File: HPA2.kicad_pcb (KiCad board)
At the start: 2 copper layers, 101.6 x 73 mm, 120 parts, among them J1 Input, J2 Conn_01x01_Male, J3 Power, J4 Output, J5 Mute, K1 G6H-2, Q1 BC560C, Q10 BC560C, Q11 BC560C, Q12 BC550C, Q13 BC550C, Q14 KSC1845, Q15 BC550C, Q16 BC560C, Q17 KSA992, Q18 BC560C, Q19 BC550C, Q2 BC560C, Q20 BC560C, Q21 BC550C, Q22 TTA004B, Q23 TTA004B, Q24 TTC004B, Q25 TTC004B, Q26 KSC2690AY, Q27 KSA1220AY, Q3 BC549C, Q4 BC549C, Q5 BC549C, Q6 BC560C, Q7 BC549C, Q8 BC560C, Q9 BC560C, U1 2N5564, U2 LT1761-BYP, U3 LT1964-BYP, U4 ADA4627-1

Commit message: Copied TO-126-3-Vertical footprint into project-local library and updated board.
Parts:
- Q22, Q23, Q24, Q25, Q26, Q27: footprint Package_TO_SOT_THT:TO-126-3_Vertical -> HPA2-footprints:TO-126-3_Vertical
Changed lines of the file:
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@@
 		)
 	)
-	(footprint "Package_TO_SOT_THT:TO-126-3_Vertical"
+	(footprint "HPA2-footprints:TO-126-3_Vertical"
 		(layer "F.Cu")
 		(at 163.195 124.46 90)
@@
 		)
 	)
-	(footprint "Package_TO_SOT_THT:TO-126-3_Vertical"
+	(footprint "HPA2-footprints:TO-126-3_Vertical"
 		(layer "F.Cu")
 		(at 163.195 88.9 -90)
@@
 		)
 	)
-	(footprint "Package_TO_SOT_THT:TO-126-3_Vertical"
+	(footprint "HPA2-footprints:TO-126-3_Vertical"
 		(layer "F.Cu")
 		(at 180.34 129.54 -90)
@@
 		)
 	)
-	(footprint "Package_TO_SOT_THT:TO-126-3_Vertical"
+	(footprint "HPA2-footprints:TO-126-3_Vertical"
 		(layer "F.Cu")
 		(at 180.34 116.84 -90)
@@
 		)
 	)
-	(footprint "Package_TO_SOT_THT:TO-126-3_Vertical"
+	(footprint "HPA2-footprints:TO-126-3_Vertical"
 		(layer "F.Cu")
 		(at 180.34 78.74 -90)
@@
 		(tags "TO-126-3 Vertical RM 2.54mm")
 		(property "Reference" "Q27"
-			(at 2.794 2.286 270)
+			(at 2.794 2.286 90)
 			(layer "F.SilkS")
 			(effects
@@
 		)
 		(property "Datasheet" ""
-			(at 0 0 270)
+			(at 0 0 90)
 			(layer "F.Fab")
 			(hide yes)
@@
 		)
 		(property "Description" ""
-			(at 0 0 270)
+			(at 0 0 90)
 			(layer "F.Fab")
 			(hide yes)
@@
 		)
 	)
-	(footprint "Package_TO_SOT_THT:TO-126-3_Vertical"
+	(footprint "HPA2-footprints:TO-126-3_Vertical"
 		(layer "F.Cu")
 		(at 180.34 91.44 -90)

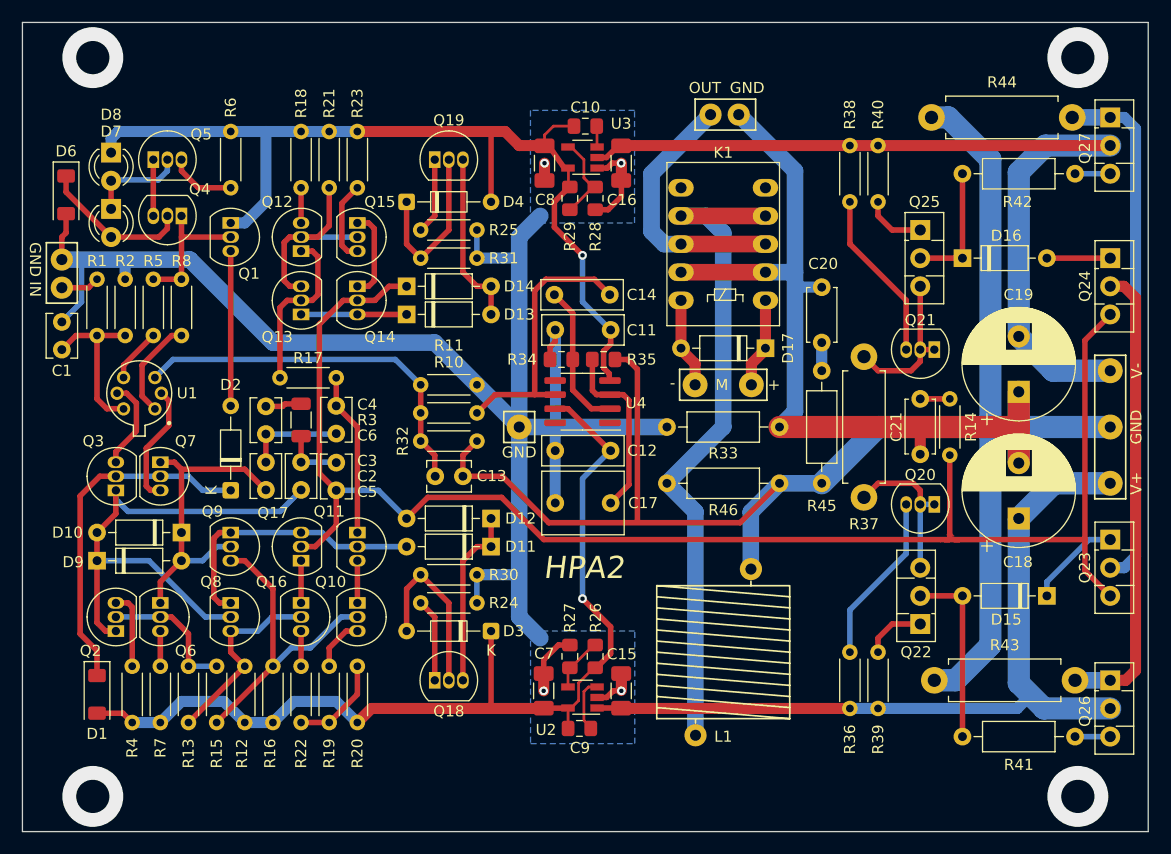
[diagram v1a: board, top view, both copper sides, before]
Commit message: Updated remaining footprints from library except for Resistor_SMD:R_0805_2012Metric_Pad1.15x1.40mm_HandSolder.
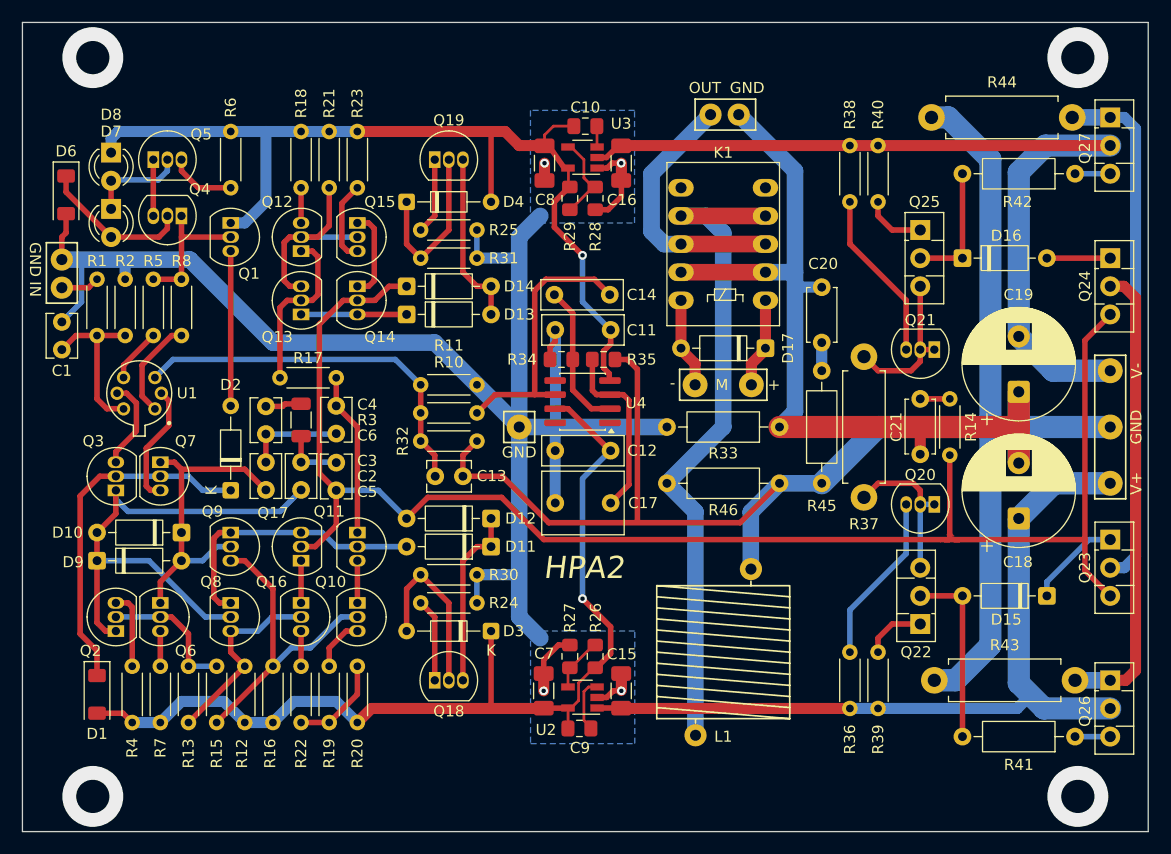
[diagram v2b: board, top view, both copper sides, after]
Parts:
- C10, C9: footprint Capacitor_SMD:C_0805_2012Metric_Pad1.15x1.40mm_HandSolder -> Capacitor_SMD:C_0805_2012Metric_Pad1.18x1.45mm_HandSolder
- D10, D11, D12, D13, D14, D15, D16, D17, D9: footprint Diode_THT:D_DO-35_SOD27_P7.62mm_Horizontal -> HPA2-footprints:D_DO-35_SOD27_P7.62mm_Horizontal

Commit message: Vendored Resistor_SMD:R_0805_2012Metric_Pad1.15x1.40mm_HandSolder. Updated board.
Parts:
- R26, R27, R28, R29, R34, R35: footprint Resistor_SMD:R_0805_2012Metric_Pad1.15x1.40mm_HandSolder -> HPA2-footprints:R_0805_2012Metric_Pad1.15x1.40mm_HandSolder
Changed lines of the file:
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@@
 	(net 81 "Net-(Q27-Pad3)")
 	(net 82 "Net-(C21-Pad1)")
-	(footprint "Resistor_SMD:R_0805_2012Metric_Pad1.15x1.40mm_HandSolder"
+	(footprint "HPA2-footprints:R_0805_2012Metric_Pad1.15x1.40mm_HandSolder"
 		(layer "F.Cu")
 		(at 134.62 100.584 180)
@@
 		)
 	)
-	(footprint "Resistor_SMD:R_0805_2012Metric_Pad1.15x1.40mm_HandSolder"
+	(footprint "HPA2-footprints:R_0805_2012Metric_Pad1.15x1.40mm_HandSolder"
 		(layer "F.Cu")
 		(at 133.858 86.0425 90)
@@
 		)
 	)
-	(footprint "Resistor_SMD:R_0805_2012Metric_Pad1.15x1.40mm_HandSolder"
+	(footprint "HPA2-footprints:R_0805_2012Metric_Pad1.15x1.40mm_HandSolder"
 		(layer "F.Cu")
 		(at 131.572 86.0425 90)
@@
 		)
 	)
-	(footprint "Resistor_SMD:R_0805_2012Metric_Pad1.15x1.40mm_HandSolder"
+	(footprint "HPA2-footprints:R_0805_2012Metric_Pad1.15x1.40mm_HandSolder"
 		(layer "F.Cu")
 		(at 133.858 127.381 90)
@@
 		)
 	)
-	(footprint "Resistor_SMD:R_0805_2012Metric_Pad1.15x1.40mm_HandSolder"
+	(footprint "HPA2-footprints:R_0805_2012Metric_Pad1.15x1.40mm_HandSolder"
 		(layer "F.Cu")
 		(at 131.572 127.381 90)
@@
 		(embedded_fonts no)
 	)
-	(footprint "Resistor_SMD:R_0805_2012Metric_Pad1.15x1.40mm_HandSolder"
+	(footprint "HPA2-footprints:R_0805_2012Metric_Pad1.15x1.40mm_HandSolder"
 		(layer "F.Cu")
 		(at 130.81 100.584)

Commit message: Updated schematic to be consistent with PCB footprint changes.
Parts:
- C4: value 150nF -> 100nF
- D1, D6: footprint HP_Footprints:Semitec-CRD-SMD -> HPA2-footprints:Semitec-CRD-SMD
- D15, D16: value 1N4148 -> BAV21
- J1, J4: footprint HP_Footprints:2-pad-wire-connector-small -> HPA2-footprints:2-pad-wire-connector-small
- J2: footprint HP_Footprints:1-pad-wire-connector-22-ga -> HPA2-footprints:1-pad-wire-connector-22-ga
- J3: footprint HP_Footprints:3-pad-wire-connector-22-ga -> HPA2-footprints:3-pad-wire-connector-22-ga
- J5: footprint HP_Footprints:2-pad-wire-connector-22-ga -> HPA2-footprints:2-pad-wire-connector-22-ga
- K1: value G6H-2 -> EA2-12NJ
- Q12, Q13, Q15: value BC550C -> BC549C
- Q2, Q6: value BC560C -> BC559C
- R37: value 3.3K 2W -> 2.2K 2W
- R41, R42: value 100R -> 10R
- U1: footprint HP_Footprints:TO-71-6 -> HPA2-footprints:TO-71-6
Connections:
- K1 pad 5: Net-(K1-Pad5) -> unconnected-(K1-NC-Pad5)
- K1 pad 6: Net-(K1-Pad6) -> unconnected-(K1-NC-Pad6)
- U4 pad 1: Net-(U4-Pad1) -> unconnected-(U4-N-Pad1)
- U4 pad 5: Net-(U4-Pad5) -> unconnected-(U4-N-Pad5)
